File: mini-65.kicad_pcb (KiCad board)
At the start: 2 copper layers, 303.5 x 94 mm, 170 parts, among them J1 TYPE-C-31-M12_13_EDITED, J2 AVR-ISP-6, SW1 SW_Push, U1 ATmega32U4-AU, U2 USBLC6-2SC6, Y1 Crystal_GND24_Small

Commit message: Updated PCB to tweaked footprints
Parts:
- D1, D10, D11, D12, D13, D14, D15, D16, D17, D18, D19, D2, D20, D21, D22, D23, D24, D25, D26, D27, D28, D29, D3, D30, D31, D32, D33, D34, D35, D36, D37, D38, D39, D4, D40, D41, D42, D43, D44, D45, D46, D47, D48, D49, D5, D50, D51, D52, D53, D54, D55, D56, D57, D58, D59, D6, D60, D61, D62, D63, D64, D65, D66, D67, D68, D69, D7, D8, D9: footprint canadian_footprints:D_SOD123_axial-dual -> mini-general-tweaks:D_SOD123_axial-dual
- H0, H1, H2, H3, H4, H5: footprint MountingHole:MountingHole_2.2mm_M2_Pad -> mini-general-tweaks:MountingHole_2.2mm_M2_Pad_tweaked
- J2: footprint Connector_PinHeader_2.54mm:PinHeader_2x03_P2.54mm_Vertical -> mini-general-tweaks:PinHeader_2x03_P2.54mm_Vertical_ICSP
- U1: footprint Package_QFP:TQFP-44_10x10mm_P0.8mm -> mini-general-tweaks:TQFP-44_10x10mm_P0.8mm_ATmega32U4
- U2: footprint Package_TO_SOT_SMD:SOT-23-6 -> mini-general-tweaks:SOT-23-6_tweaked

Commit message: Tweaked footprints
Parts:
- moved SW1 2.67 mm to (35.7, 167.8)
- moved F1 1.19 mm to (-66.4, 93.6)
- moved J1 1.19 mm to (-60.8, 78.9)
- moved R5 1.19 mm to (-64.0, 93.4)
- moved R6 1.19 mm to (-57.8, 93.4)
- moved R2 1.19 mm to (-59.7, 97.9)
- moved R3 1.19 mm to (-62.0, 97.9)
- moved U2 1.19 mm to (-60.8, 93.2)
- moved J2 0.79 mm to (34.1, 157.2)
- moved R1 0.25 mm to (31.6, 153.4), turned to 0 degrees
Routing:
- net ROW4: track 248.0 -> 290.1 mm
- net GND: track 1005.6 -> 976.6 mm
- net RESET: track 41.4 -> 44.3 mm
- net +5V: track 231.1 -> 230.0 mm
- net DN: track 138.2 -> 137.3 mm
- net DP: track 137.9 -> 137.0 mm
- net ROW1: track 338.0 -> 338.8 mm
- net ROW0: track 574.0 -> 574.7 mm

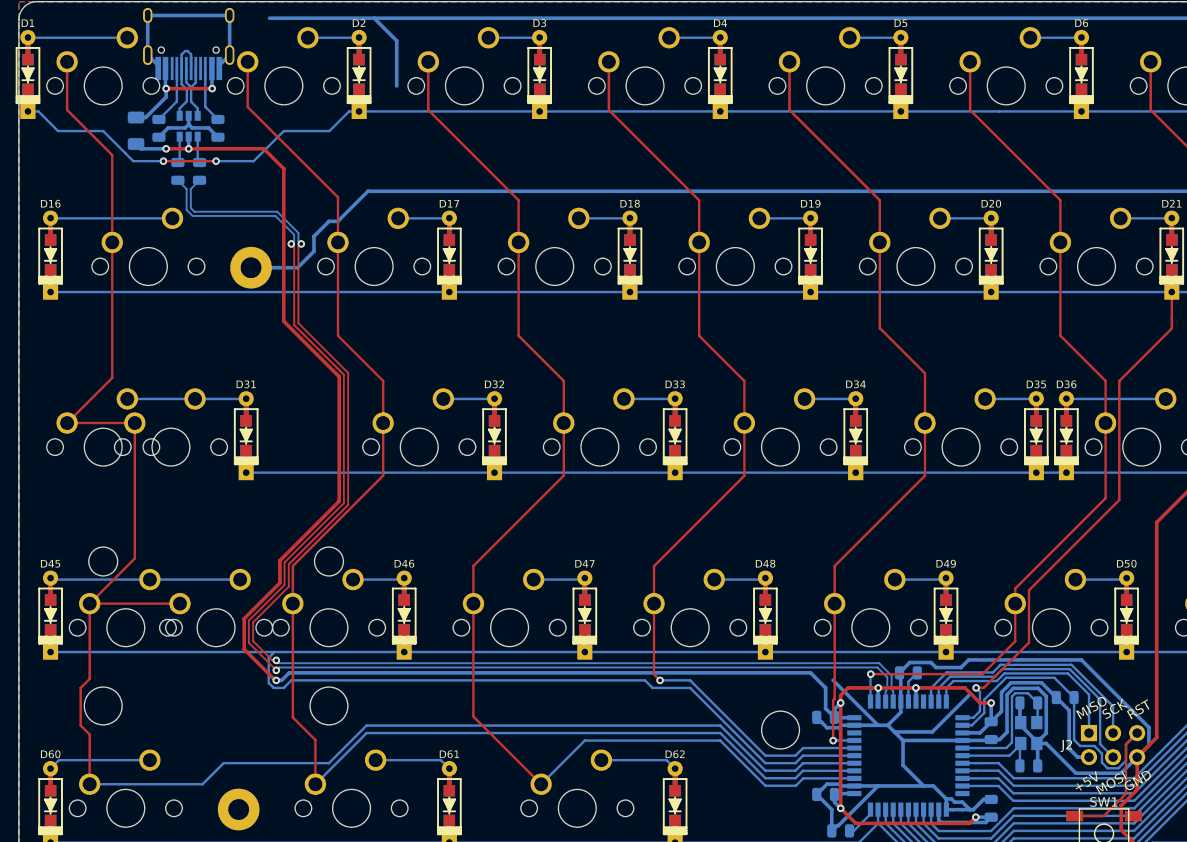
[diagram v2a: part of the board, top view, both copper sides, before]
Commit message: Restructured USB area, general silkscreen tweaks
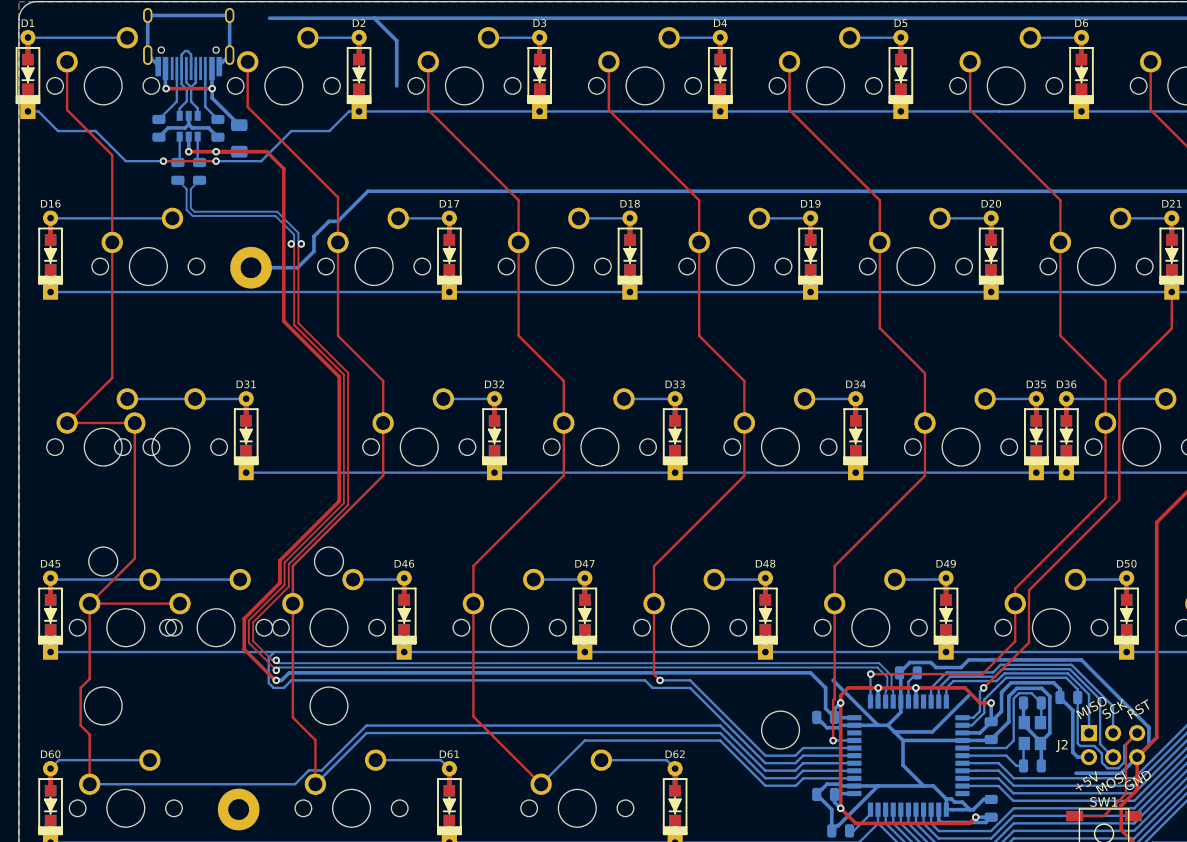
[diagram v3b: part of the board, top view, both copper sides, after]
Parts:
- J1: footprint Type-C:HRO-TYPE-C-31-M-12-HandSoldering -> mini-general-tweaks:HRO-TYPE-C-31-M-12-HandSoldering_tweaked
- moved F1 10.9 mm to (-55.5, 94.4)
- moved C1 0.38 mm to (28.2, 160.6)
- moved C2 0.38 mm to (28.2, 154.0)
- moved Y1 0.38 mm to (28.2, 157.2)
- moved R1 0.38 mm to (32.0, 153.4)
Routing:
- net GND: track 976.6 -> 970.8 mm
- net +5V: track 230.0 -> 227.6 mm
- net ROW1: track 338.8 -> 338.0 mm
- net RESET: track 44.3 -> 45.0 mm

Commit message: Added annotations under some multi compatibility keys
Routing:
- net GND: track 970.8 -> 967.2 mm
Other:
- board text added: "1.25U"
- board text added: "1U"
- board text added: "ANSI ENTER"
- board text added: "ANSI SHIFT"
- board text added: "ANSI \"
- board text added: "CAPS"
- board text added: "ISO ENTER"
- board text added: "ISO SHIFT"
- board text added: "ISO \"
- board text added: "STEPPED CAPS"
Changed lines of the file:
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@@
   (general
     (thickness 1.6)
-    (drawings 8)
-    (tracks 995)
+    (drawings 22)
+    (tracks 987)
     (zones 0)
     (modules 170)
@@
     )
   )
+  (gr_text 1U (at 151.892 168.148) (layer F.SilkS)
+    (effects (font (size 1 1) (thickness 0.15)))
+  )
+  (gr_text 1.25U (at 140.462 168.148) (layer F.SilkS)
+    (effects (font (size 1 1) (thickness 0.15)))
+  )
+  (gr_text 1U (at 136.652 168.148) (layer F.SilkS)
+    (effects (font (size 1 1) (thickness 0.15)))
+  )
+  (gr_text 1.25U (at 123.952 168.148) (layer F.SilkS)
+    (effects (font (size 1 1) (thickness 0.15)))
+  )
+  (gr_text 1U (at 120.142 168.148) (layer F.SilkS)
+    (effects (font (size 1 1) (thickness 0.15)))
+  )
+  (gr_text "ANSI \\" (at 192.15 110.8) (layer F.SilkS)
+    (effects (font (size 1 1) (thickness 0.15)))
+  )
+  (gr_text "ISO\nENTER" (at 189.865 117.475) (layer F.SilkS)
+    (effects (font (size 1 1) (thickness 0.15)))
+  )
+  (gr_text "ISO \\" (at 172.847 129.875) (layer F.SilkS)
+    (effects (font (size 1 1) (thickness 0.15)))
+  )
+  (gr_text "ANSI\nENTER" (at 185.166 133.096) (layer F.SilkS)
+    (effects (font (size 1 1) (thickness 0.15)))
+  )
+  (gr_text CAPS (at -62.5856 129.98704) (layer F.SilkS)
+    (effects (font (size 1 1) (thickness 0.15)))
+  )
+  (gr_text "STEPPED\nCAPS" (at -69.85 130.81) (layer F.SilkS)
+    (effects (font (size 1 1) (thickness 0.15)))
+  )
+  (gr_text "ISO \\" (at -45.875 148.9) (layer F.SilkS)
+    (effects (font (size 1 1) (thickness 0.15)))
+  )
+  (gr_text "ISO\nSHIFT" (at -67.437 149.733) (layer F.SilkS)
+    (effects (font (size 1 1) (thickness 0.15)))
+  )
+  (gr_text "ANSI\nSHIFT" (at -57.912 149.733) (layer F.SilkS)
+    (effects (font (size 1 1) (thickness 0.15)))
+  )
   (gr_line (start -76.835 173.99) (end 222.885 173.99) (layer Edge.Cuts) (width 0.05))
   (gr_line (start 222.885 80.01) (end -76.835 80.01) (layer Edge.Cuts) (width 0.05))
@@
   (segment (start -60.833 92.0545) (end -60.833 92.9655) (width 0.381) (layer B.Cu) (net 1))
   (segment (start -65.153 81.467) (end -56.513 81.467) (width 0.381) (layer B.Cu) (net 1))
-  (segment (start 19.08125 164.11275) (end 19.08125 165.24375) (width 0.381) (layer B.Cu) (net 1))
-  (segment (start 17.71225 162.74375) (end 19.08125 164.11275) (width 0.381) (layer B.Cu) (net 1))
   (segment (start 14.28125 154.97475) (end 14.28125 153.84375) (width 0.381) (layer B.Cu) (net 1))
   (segment (start 12.91225 156.34375) (end 14.28125 154.97475) (width 0.381) (layer B.Cu) (net 1))
@@
   (segment (start 14.51225 160.56225) (end 16.69375 162.74375) (width 0.381) (layer B.Cu) (net 1))
   (segment (start 11.88125 162.74375) (end 16.69375 162.74375) (width 0.381) (layer B.Cu) (net 1))
-  (segment (start 16.69375 162.74375) (end 17.71225 162.74375) (width 0.381) (layer B.Cu) (net 1))
   (segment (start 5.968737 156.067737) (end 5.4125 155.5115) (width 0.381) (layer B.Cu) (net 1))
   (segment (start 6.50301 156.60201) (end 5.968737 156.067737) (width 0.381) (layer B.Cu) (net 1))
@@
   (segment (start 49.2125 120.65) (end 53.18125 116.68125) (width 0.381) (layer B.Cu) (net 1))
   (segment (start 49.2125 127) (end 49.2125 120.65) (width 0.381) (layer B.Cu) (net 1))
-  (segment (start 19.73725 165.24375) (end 19.08125 165.24375) (width 0.381) (layer B.Cu) (net 1))
-  (segment (start 23.0125 164.1625) (end 21.93125 165.24375) (width 0.381) (layer B.Cu) (net 1))
-  (segment (start 23.8125 164.1625) (end 23.0125 164.1625) (width 0.381) (layer B.Cu) (net 1))
   (segment (start 14.28125 150.95) (end 14.28125 153.84375) (width 0.381) (layer B.Cu) (net 1))
   (segment (start 14.14375 150.8125) (end 14.28125 150.95) (width 0.381) (layer B.Cu) (net 1))
@@
   (segment (start 7.556237 166.925013) (end 7.699987 166.925013) (width 0.381) (layer B.Cu) (net 1))
   (segment (start 7 167.48125) (end 7.556237 166.925013) (width 0.381) (layer B.Cu) (net 1))
-  (segment (start 20.78125 165.24375) (end 19.73725 165.24375) (width 0.381) (layer B.Cu) (net 1))
-  (segment (start 19.622348 164.11275) (end 19.08125 164.11275) (width 0.381) (layer B.Cu) (net 1))
-  (segment (start 19.959598 164.45) (end 19.622348 164.11275) (width 0.381) (layer B.Cu) (net 1))
-  (segment (start 20.78125 164.45) (end 19.959598 164.45) (width 0.381) (layer B.Cu) (net 1))
-  (segment (start 20.78125 164.45) (end 21.575 165.24375) (width 0.381) (layer B.Cu) (net 1))
-  (segment (start 21.93125 165.24375) (end 21.575 165.24375) (width 0.381) (layer B.Cu) (net 1))
-  (segment (start 21.575 165.24375) (end 20.78125 165.24375) (width 0.381) (layer B.Cu) (net 1))
   (segment (start -41.275 81.75625) (end 168.275 81.75625) (width 0.381) (layer B.Cu) (net 1))
   (segment (start 180.975 81.75625) (end 191.29375 81.75625) (width 0.381) (layer B.Cu) (net 1))
@@
   (segment (start 25.67624 155.98226) (end 25.67624 153.296963) (width 0.381) (layer B.Cu) (net 1))
   (segment (start 23.8125 157.846) (end 25.67624 155.98226) (width 0.381) (layer B.Cu) (net 1))
+  (segment (start 23.0125 164.1625) (end 23.8125 164.1625) (width 0.381) (layer B.Cu) (net 1))
+  (segment (start 21.93125 165.24375) (end 23.0125 164.1625) (width 0.381) (layer B.Cu) (net 1))
+  (segment (start 20.753348 165.24375) (end 21.93125 165.24375) (width 0.381) (layer B.Cu) (net 1))
+  (segment (start 16.69375 162.74375) (end 18.253348 162.74375) (width 0.381) (layer B.Cu) (net 1))
+  (segment (start 18.253348 162.74375) (end 20.753348 165.24375) (width 0.381) (layer B.Cu) (net 1))
   (segment (start 27.22475 158.346856) (end 27.31225 158.259356) (width 0.254) (layer B.Cu) (net 2))
   (segment (start 27.22475 160.334357) (end 27.22475 158.346856) (width 0.254) (layer B.Cu) (net 2))

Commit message: general edits
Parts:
- moved R4 1.80 mm to (6.35, 166.6)
- moved D69 1.05 mm to (208.0, 163.8)
- moved D67 1.05 mm to (169.9, 163.8)
- moved D60 1.05 mm to (-75.4, 163.8)
- moved D61 1.05 mm to (-33.3, 163.8)
- moved D62 1.05 mm to (-9.53, 163.8)
- moved D63 1.05 mm to (59.6, 163.8)
- moved D64 1.05 mm to (112.7, 163.8)
- moved D65 1.05 mm to (131.8, 163.8)
- moved D66 1.05 mm to (166.7, 163.8)
- moved D68 1.05 mm to (204.8, 163.8)
- moved H1 0.69 mm to (-55.0, 164.8)
- moved J1 0.52 mm to (-61.0, 78.4)
- moved R5 0.52 mm to (-64.1, 92.9)
- moved U2 0.52 mm to (-61.0, 92.6)
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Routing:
- net GND: track 967.2 -> 611.0 mm
- net VCC: track 14.1 -> 15.5 mm
- net Net-(R4-Pad2): track 3.41 -> 4.64 mm
- net DP: track 137.0 -> 137.6 mm
- net DN: track 137.3 -> 137.8 mm

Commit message: step before flipping all diodes
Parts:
- moved D50 10.3 mm to (30.2, 138.0), turned to 180 degrees
- moved D60 1.08 mm to (-75.4, 164.8)
- moved D61 1.08 mm to (-33.3, 164.8)
- moved D62 1.08 mm to (-9.53, 164.8)
- moved D63 1.08 mm to (59.6, 164.8)
- moved D64 1.08 mm to (112.7, 164.8)
- moved D65 1.08 mm to (131.8, 164.8)
- moved D66 1.08 mm to (166.7, 164.8)
- moved D67 1.08 mm to (169.9, 164.8)
- moved D68 1.08 mm to (204.8, 164.8)
- moved D69 1.08 mm to (208.0, 164.8)
- turned C5 to 270 degrees
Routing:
- net GND: track 611.0 -> 185.2 mm
- net Net-(D36-Pad2): track 10.5 -> 0.00 mm
- net Net-(D1-Pad2): track 10.5 -> 0.00 mm
- net Net-(D50-Pad2): track 5.68 -> 0.00 mm
- net Net-(D57-Pad2): track 5.46 -> 0.00 mm
- net Net-(D56-Pad2): track 5.68 -> 0.22 mm
- net Net-(D52-Pad2): track 5.68 -> 0.22 mm
- net Net-(D47-Pad2): track 5.68 -> 0.22 mm
- net Net-(D51-Pad2): track 5.68 -> 0.22 mm
- net Net-(D49-Pad2): track 5.68 -> 0.22 mm
- net Net-(D46-Pad2): track 5.68 -> 0.22 mm
- net Net-(D48-Pad2): track 5.68 -> 0.22 mm
- net Net-(D53-Pad2): track 5.68 -> 0.22 mm
- net Net-(D55-Pad2): track 5.68 -> 0.22 mm
- net Net-(D54-Pad2): track 5.66 -> 0.20 mm
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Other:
- board size 303.5 x 94 mm -> 302.8 x 94 mm

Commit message: Diodes in different place, row traces mostly ran.
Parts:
- moved D43 21.0 mm to (184.9, 119.1), turned to 0 degrees
- moved D14 19.7 mm to (187.3, 96.8), turned to 0 degrees
- moved D45 18.7 mm to (-57.9, 138.1), turned to 0 degrees
- moved D29 14.1 mm to (192.1, 100.0), turned to 0 degrees
- moved D62 12.9 mm to (-19.8, 157.2), turned to 0 degrees
- moved D61 12.9 mm to (-43.7, 157.2), turned to 0 degrees
- moved D1 12.1 mm to (-69.8, 96.8), turned to 0 degrees
- moved D10 12.1 mm to (101.6, 96.8), turned to 0 degrees
- moved D11 12.1 mm to (120.7, 96.8), turned to 0 degrees
- moved D12 12.1 mm to (139.7, 96.8), turned to 0 degrees
- moved D13 12.1 mm to (158.8, 96.8), turned to 0 degrees
- moved D15 12.1 mm to (215.9, 96.8), turned to 0 degrees
- moved D2 12.1 mm to (-50.8, 96.8), turned to 0 degrees
- moved D3 12.1 mm to (-31.8, 96.8), turned to 0 degrees
- moved D4 12.1 mm to (-12.7, 96.8), turned to 0 degrees
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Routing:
- net ROW4: track 290.1 -> 192.2 mm
- net COL14: track 278.8 -> 189.0 mm
- net COL0: track 185.1 -> 116.0 mm
- net GND: track 185.2 -> 123.9 mm
- net COL1: track 148.4 -> 103.5 mm
- net ROW1: track 338.0 -> 365.4 mm
- net COL2: track 126.3 -> 105.5 mm
- net ROW2: track 505.5 -> 522.0 mm
- net Net-(D43-Pad2): track 31.5 -> 15.3 mm
- net COL7: track 122.2 -> 106.4 mm
- net COL8: track 141.6 -> 126.9 mm
- net RESET: track 45.0 -> 30.5 mm
- net ROW3: track 353.2 -> 367.6 mm
- net Net-(D13-Pad2): track 0.00 -> 13.6 mm
- net Net-(D9-Pad2): track 0.00 -> 13.6 mm
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
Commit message: ran most column/row wires. about to change schematic
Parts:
- moved D65 14.8 mm to (144.5, 157.2), turned to 0 degrees
- moved D64 12.2 mm to (122.2, 157.2), turned to 0 degrees
- moved D67 11.0 mm to (177.8, 157.2), turned to 0 degrees
- moved D66 11.0 mm to (158.8, 157.2), turned to 0 degrees
- moved D68 11.0 mm to (196.8, 157.2), turned to 0 degrees
- moved D69 8.64 mm to (211.9, 157.2), turned to 0 degrees
- moved D15 3.97 mm to (211.9, 96.8)
- moved D30 3.97 mm to (211.9, 100.0)
- moved D44 3.97 mm to (211.9, 119.1)
- moved D59 3.97 mm to (211.9, 138.1)
- moved C5 1.42 mm to (24.3, 166.0), turned to 0 degrees
- moved C4 0.48 mm to (24.3, 156.7), turned to 0 degrees
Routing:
- net COL6: track 131.8 -> 341.2 mm
- net ROW0: track 580.9 -> 430.2 mm
- net ROW2: track 522.0 -> 392.4 mm
- net COL2: track 105.5 -> 235.0 mm
- net ROW4: track 192.2 -> 314.4 mm
- net COL1: track 103.5 -> 184.8 mm
- net COL9: track 232.6 -> 310.7 mm
- net COL0: track 116.0 -> 169.0 mm, vias 0 -> 1
- net COL10: track 261.7 -> 314.0 mm
- net COL11: track 238.9 -> 286.2 mm
- net COL13: track 271.5 -> 228.3 mm
- net COL14: track 189.0 -> 150.1 mm
- net ROW3: track 367.6 -> 345.8 mm, vias 0 -> 1
- net ROW1: track 365.4 -> 386.1 mm
- net COL12: track 279.8 -> 267.2 mm
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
